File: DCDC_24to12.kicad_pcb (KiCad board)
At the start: 2 copper layers, 26 parts, among them J1 Power_IN, J2 Power_OUT, U1 BD9F800MUX-ZE2

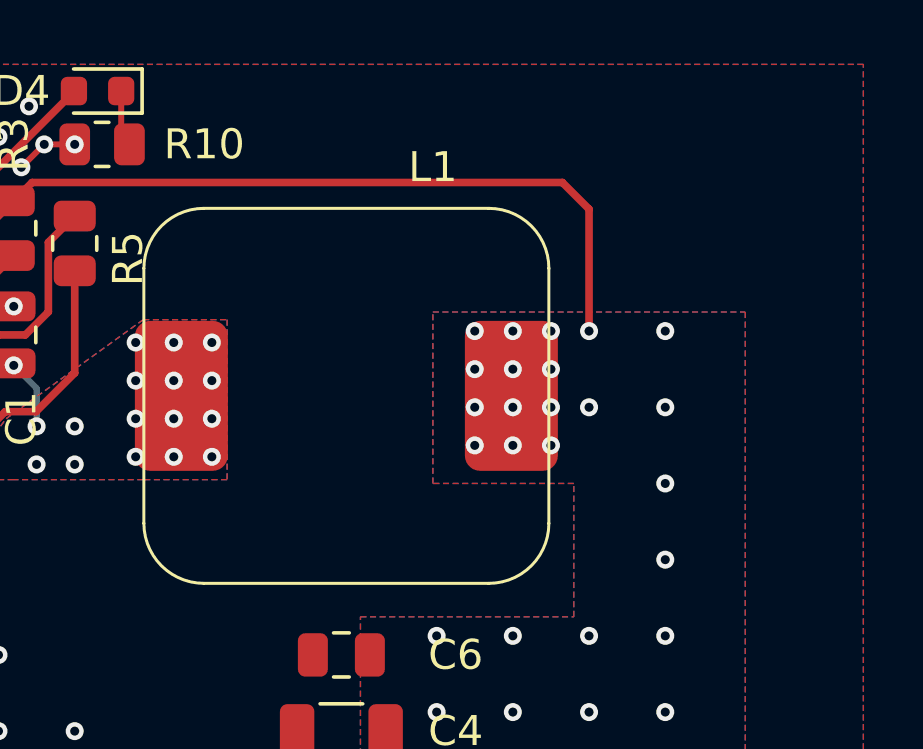
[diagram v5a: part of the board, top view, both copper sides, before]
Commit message: 制御へのGNDにビア追加
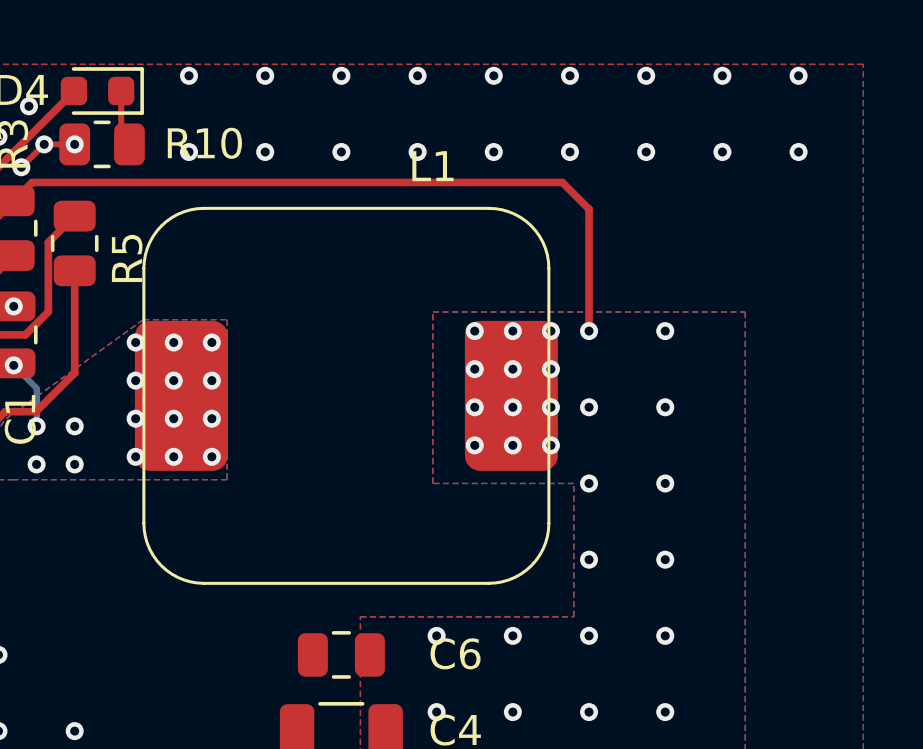
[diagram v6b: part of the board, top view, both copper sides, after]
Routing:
- net GND: vias 78 -> 96
- net +12V: vias 30 -> 32
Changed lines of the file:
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@@
+	)
+	(via
+		(at 113.03 44.196)
+		(size 0.6)
+		(drill 0.3)
+		(layers "F.Cu" "B.Cu")
+		(free yes)
+		(net 1)
 	)
 	(via
@@
 	)
 	(via
+		(at 115.57 44.196)
+		(size 0.6)
+		(drill 0.3)
+		(layers "F.Cu" "B.Cu")
+		(free yes)
+		(net 1)
+	)
+	(via
 		(at 104.14 43.688)
 		(size 0.6)
@@
 	)
 	(via
+		(at 123.19 44.196)
+		(size 0.6)
+		(drill 0.3)
+		(layers "F.Cu" "B.Cu")
+		(free yes)
+		(net 1)
+	)
+	(via
 		(at 96.52 63.5)
 		(size 0.6)
@@
 	)
 	(via
+		(at 130.81 41.656)
+		(size 0.6)
+		(drill 0.3)
+		(layers "F.Cu" "B.Cu")
+		(free yes)
+		(net 1)
+	)
+	(via
 		(at 104.902 44.704)
 		(size 0.6)
@@
 	)
 	(via
+		(at 115.57 41.656)
+		(size 0.6)
+		(drill 0.3)
+		(layers "F.Cu" "B.Cu")
+		(free yes)
+		(net 1)
+	)
+	(via
 		(at 88.9 73.66)
 		(size 0.6)
@@
 	)
 	(via
+		(at 123.19 41.656)
+		(size 0.6)
+		(drill 0.3)
+		(layers "F.Cu" "B.Cu")
+		(free yes)
+		(net 1)
+	)
+	(via
+		(at 113.03 41.656)
+		(size 0.6)
+		(drill 0.3)
+		(layers "F.Cu" "B.Cu")
+		(free yes)
+		(net 1)
+	)
+	(via
 		(at 93.98 60.96)
 		(size 0.6)
@@
 	)
 	(via
+		(at 128.27 44.196)
+		(size 0.6)
+		(drill 0.3)
+		(layers "F.Cu" "B.Cu")
+		(free yes)
+		(net 1)
+	)
+	(via
 		(at 93.98 73.66)
 		(size 0.6)
@@
 	)
 	(via
+		(at 125.73 41.656)
+		(size 0.6)
+		(drill 0.3)
+		(layers "F.Cu" "B.Cu")
+		(free yes)
+		(net 1)
+	)
+	(via
 		(at 99.06 46.99)
 		(size 0.6)
@@
 	)
 	(via
+		(at 125.73 44.196)
+		(size 0.6)
+		(drill 0.3)
+		(layers "F.Cu" "B.Cu")
+		(free yes)
+		(net 1)
+	)
+	(via
 		(at 94.488 48.26)
 		(size 0.6)
@@
 	)
 	(via
+		(at 118.11 44.196)
+		(size 0.6)
+		(drill 0.3)
+		(layers "F.Cu" "B.Cu")
+		(free yes)
+		(net 1)
+	)
+	(via
 		(at 106.68 66.04)
 		(size 0.6)
@@
 	)
 	(via
+		(at 130.81 44.196)
+		(size 0.6)
+		(drill 0.3)
+		(layers "F.Cu" "B.Cu")
+		(free yes)
+		(net 1)
+	)
+	(via
+		(at 110.49 44.196)
+		(size 0.6)
+		(drill 0.3)
+		(layers "F.Cu" "B.Cu")
+		(free yes)
+		(net 1)
+	)
+	(via
 		(at 86.36 63.5)
 		(size 0.6)
@@
 	)
 	(via
+		(at 120.65 41.656)
+		(size 0.6)
+		(drill 0.3)
+		(layers "F.Cu" "B.Cu")
+		(free yes)
+		(net 1)
+	)
+	(via
 		(at 99.06 71.12)
 		(size 0.6)
@@
 	)
 	(via
+		(at 120.65 44.196)
+		(size 0.6)
+		(drill 0.3)
+		(layers "F.Cu" "B.Cu")
+		(free yes)
+		(net 1)
+	)
+	(via
 		(at 88.9 63.5)
 		(size 0.6)
@@
 	)
 	(via
+		(at 110.49 41.656)
+		(size 0.6)
+		(drill 0.3)
+		(layers "F.Cu" "B.Cu")
+		(free yes)
+		(net 1)
+	)
+	(via
 		(at 106.68 63.5)
 		(size 0.6)
@@
 	)
 	(via
+		(at 118.11 41.656)
+		(size 0.6)
+		(drill 0.3)
+		(layers "F.Cu" "B.Cu")
+		(free yes)
+		(net 1)
+	)
+	(via
 		(at 106.68 43.942)
 		(size 0.6)
@@
 	(via
 		(at 101.6 71.12)
+		(size 0.6)
+		(drill 0.3)
+		(layers "F.Cu" "B.Cu")
+		(free yes)
+		(net 1)
+	)
+	(via
+		(at 128.27 41.656)
 		(size 0.6)
 		(drill 0.3)
@@
 	)
 	(via
+		(at 123.825 55.245)
+		(size 0.6)
+		(drill 0.3)
+		(layers "F.Cu" "B.Cu")
+		(free yes)
+		(net 2)
+	)
+	(via
 		(at 120.015 53.975)
 		(size 0.6)
@@
 		(size 0.6)
 		(drill 0.3)
+		(layers "F.Cu" "B.Cu")
+		(free yes)
+		(net 2)
+	)
+	(via
+		(at 123.825 57.785)
+		(size 0.6)
+		(drill 0.3)

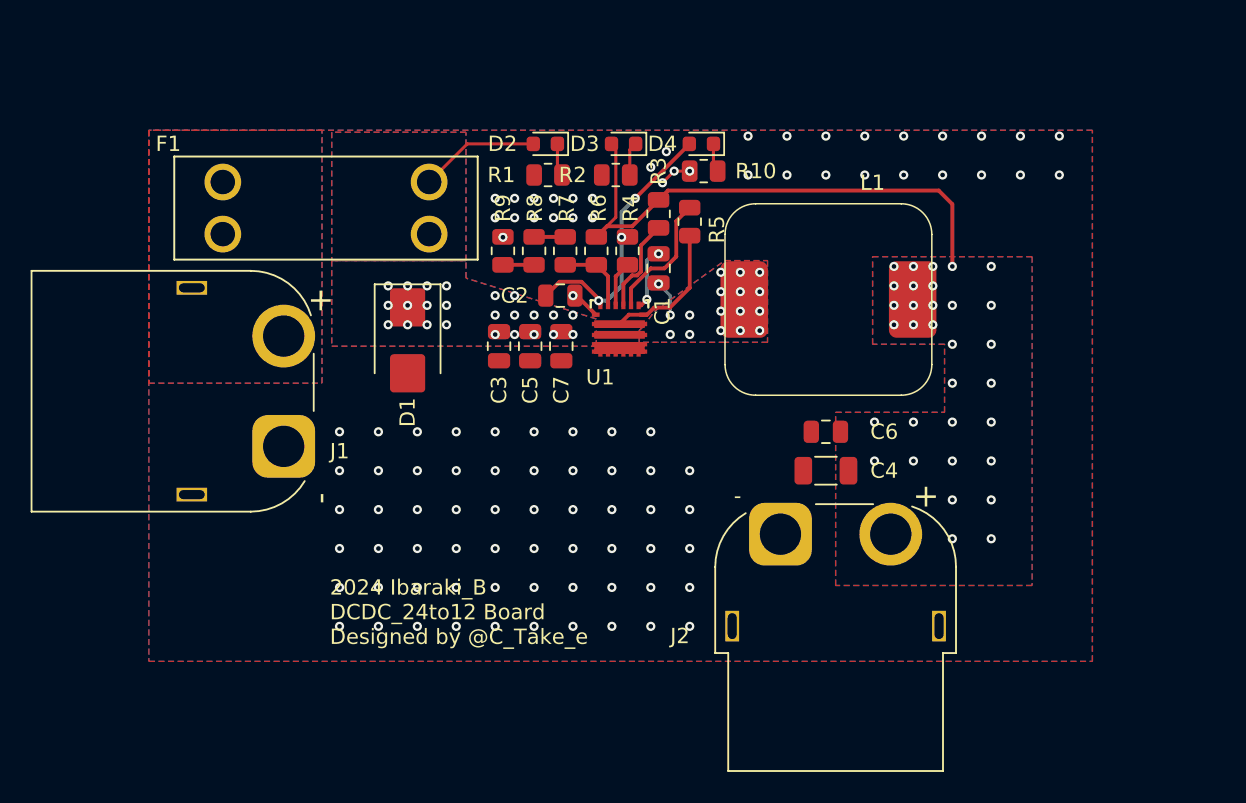
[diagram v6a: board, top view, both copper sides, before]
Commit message: LED周りGNDビア改善（改悪の可能性もある）
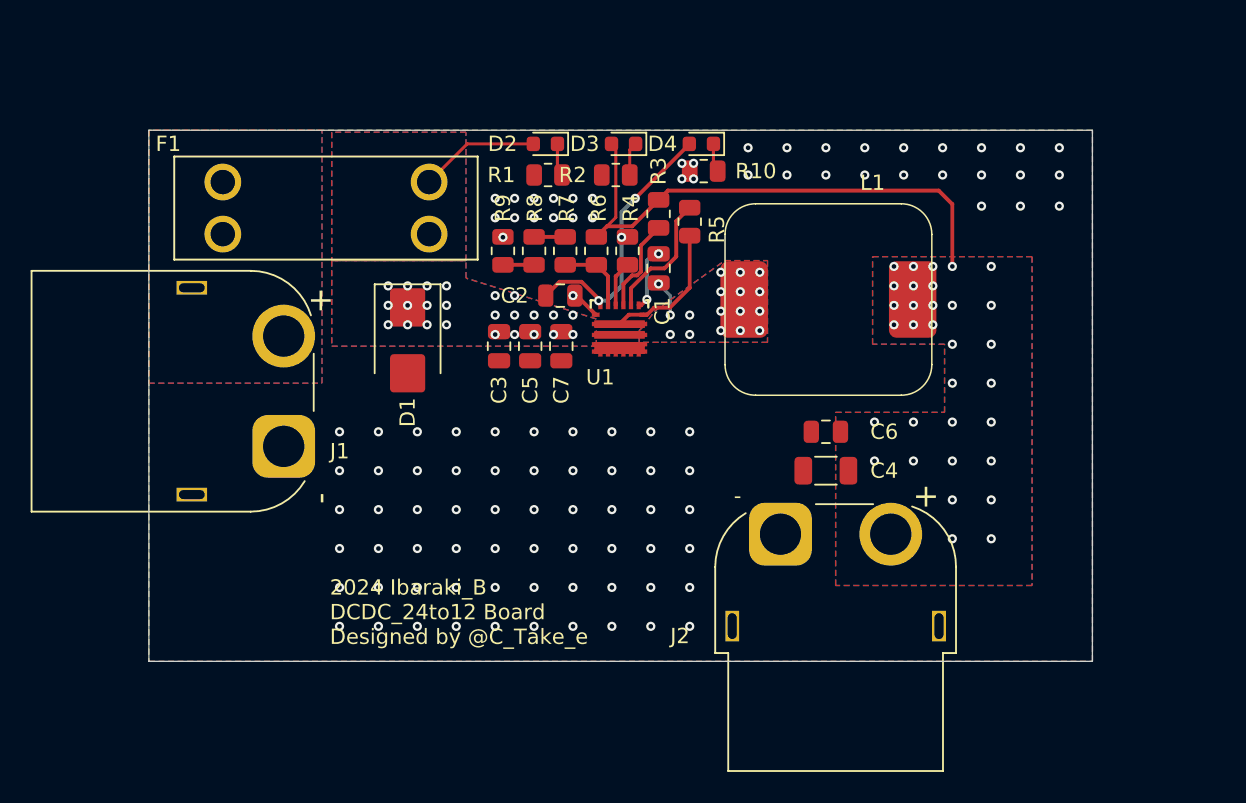
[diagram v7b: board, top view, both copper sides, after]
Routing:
- net GND: track 4.82 -> 2.73 mm, vias 96 -> 99
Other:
- board outline added: 61.6 x 34.7 mm
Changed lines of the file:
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@@
 		(layer "F.Mask")
+	)
+	(gr_rect
+		(start 71.374 41.275)
+		(end 132.969 75.946)
+		(stroke
+			(width 0.05)
+			(type default)
+		)
+		(fill none)
+		(layer "Edge.Cuts")
 	)
 	(gr_text "2024 Ibaraki_B\nDCDC_24to12 Board\nDesigned by @C_Take_e"
@@
 	)
 	(segment
-		(start 105.664 43.942)
-		(end 106.68 43.942)
-		(width 0.2)
-		(layer "F.Cu")
-		(net 1)
-	)
-	(segment
 		(start 99.302966 52.07)
 		(end 100.547965 53.314999)
@@
 	)
 	(segment
-		(start 104.902 44.704)
-		(end 105.664 43.942)
-		(width 0.2)
-		(layer "F.Cu")
-		(net 1)
-	)
-	(segment
 		(start 100.547965 53.314999)
 		(end 100.426997 53.314999)
@@
 	)
 	(via
-		(at 104.14 43.688)
-		(size 0.6)
-		(drill 0.3)
-		(layers "F.Cu" "B.Cu")
-		(free yes)
-		(net 1)
-	)
-	(via
 		(at 123.19 44.196)
 		(size 0.6)
@@
 	)
 	(via
-		(at 130.81 41.656)
-		(size 0.6)
-		(drill 0.3)
-		(layers "F.Cu" "B.Cu")
-		(free yes)
-		(net 1)
-	)
-	(via
-		(at 104.902 44.704)
+		(at 130.81 42.418)
 		(size 0.6)
 		(drill 0.3)
@@
 	)
 	(via
-		(at 115.57 41.656)
+		(at 115.57 42.418)
 		(size 0.6)
 		(drill 0.3)
@@
 	)
 	(via
+		(at 106.172 43.434)
+		(size 0.6)
+		(drill 0.3)
+		(layers "F.Cu" "B.Cu")
+		(free yes)
+		(net 1)
+	)
+	(via
 		(at 104.14 68.58)
 		(size 0.6)
@@
 	)
 	(via
+		(at 106.934 44.45)
+		(size 0.6)
+		(drill 0.3)
+		(layers "F.Cu" "B.Cu")
+		(free yes)
+		(net 1)
+	)
+	(via
 		(at 100.33 46.99)
 		(size 0.6)
@@
 	)
 	(via
-		(at 123.19 41.656)
-		(size 0.6)
-		(drill 0.3)
-		(layers "F.Cu" "B.Cu")
-		(free yes)
-		(net 1)
-	)
-	(via
-		(at 113.03 41.656)
+		(at 123.19 42.418)
+		(size 0.6)
+		(drill 0.3)
+		(layers "F.Cu" "B.Cu")
+		(free yes)
+		(net 1)
+	)
+	(via
+		(at 113.03 42.418)
 		(size 0.6)
 		(drill 0.3)
@@
 	)
 	(via
-		(at 125.73 41.656)
+		(at 125.73 42.418)
 		(size 0.6)
 		(drill 0.3)
@@
 	)
 	(via
-		(at 105.156 42.672)
-		(size 0.6)
-		(drill 0.3)
-		(layers "F.Cu" "B.Cu")
-		(free yes)
-		(net 1)
-	)
-	(via
 		(at 86.36 66.04)
 		(size 0.6)
@@
 	)
 	(via
+		(at 106.172 44.45)
+		(size 0.6)
+		(drill 0.3)
+		(layers "F.Cu" "B.Cu")
+		(free yes)
+		(net 1)
+	)
+	(via
 		(at 104.14 71.12)
 		(size 0.6)
@@
 	)
 	(via
+		(at 125.73 46.228)
+		(size 0.6)
+		(drill 0.3)
+		(layers "F.Cu" "B.Cu")
+		(free yes)
+		(net 1)
+	)
+	(via
 		(at 96.52 66.04)
 		(size 0.6)
@@
 	)
 	(via
+		(at 130.81 46.228)
+		(size 0.6)
+		(drill 0.3)
+		(layers "F.Cu" "B.Cu")
+		(free yes)
+		(net 1)
+	)
+	(via
 		(at 104.14 60.96)
 		(size 0.6)
@@
 	)
 	(via
+		(at 128.27 46.228)
+		(size 0.6)
+		(drill 0.3)
+		(layers "F.Cu" "B.Cu")
+		(free yes)
+		(net 1)
+	)
+	(via
 		(at 101.6 60.96)
 		(size 0.6)
@@
 	)
 	(via
-		(at 120.65 41.656)
+		(at 120.65 42.418)
 		(size 0.6)
 		(drill 0.3)
@@
 	)
 	(via
+		(at 106.68 60.96)
+		(size 0.6)
+		(drill 0.3)
+		(layers "F.Cu" "B.Cu")
+		(free yes)
+		(net 1)
+	)
+	(via
 		(at 99.06 63.5)
 		(size 0.6)
@@
 	)
 	(via
-		(at 110.49 41.656)
+		(at 110.49 42.418)
 		(size 0.6)
 		(drill 0.3)
@@
 	)
 	(via
-		(at 118.11 41.656)
-		(size 0.6)
-		(drill 0.3)
-		(layers "F.Cu" "B.Cu")
-		(free yes)
-		(net 1)
-	)
-	(via
-		(at 106.68 43.942)
+		(at 118.11 42.418)
+		(size 0.6)
+		(drill 0.3)
+		(layers "F.Cu" "B.Cu")
+		(free yes)
+		(net 1)
+	)
+	(via
+		(at 106.934 43.434)
 		(size 0.6)
 		(drill 0.3)
@@
 	)
 	(via
-		(at 128.27 41.656)
+		(at 128.27 42.418)
 		(size 0.6)
 		(drill 0.3)
@@
 		(size 0.6)
 		(drill 0.3)
-		(layers "F.Cu" "B.Cu")
-		(free yes)
-		(net 1)
-	)
-	(via
-		(at 105.664 43.942)
-		(size 0.6)
-		(drill 0.3)

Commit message: ビアボー
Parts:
- moved R10 1.79 mm to (108.7, 42.5)
- moved R2 1.61 mm to (102.4, 42.7)
- moved R1 1.53 mm to (97.3, 42.7)
- moved D2 1.52 mm to (97.3, 40.6)
- moved D3 1.52 mm to (102.4, 40.6)
- moved D4 1.52 mm to (107.4, 40.6)
- moved C6 0.51 mm to (116.1, 61.0)
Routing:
- net VREG: track 17.8 -> 20.0 mm
- net +12V: track 34.7 -> 36.6 mm
- net +BATT: track 16.8 -> 17.4 mm
- net Net-(D4-K): track 1.89 -> 2.48 mm
- net GND: track 2.73 -> 2.94 mm, vias 99 -> 129
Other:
- board size 61.6 x 34.7 mm -> 61.6 x 36.7 mm
